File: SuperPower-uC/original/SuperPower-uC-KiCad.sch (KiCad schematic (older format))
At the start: 0 parts

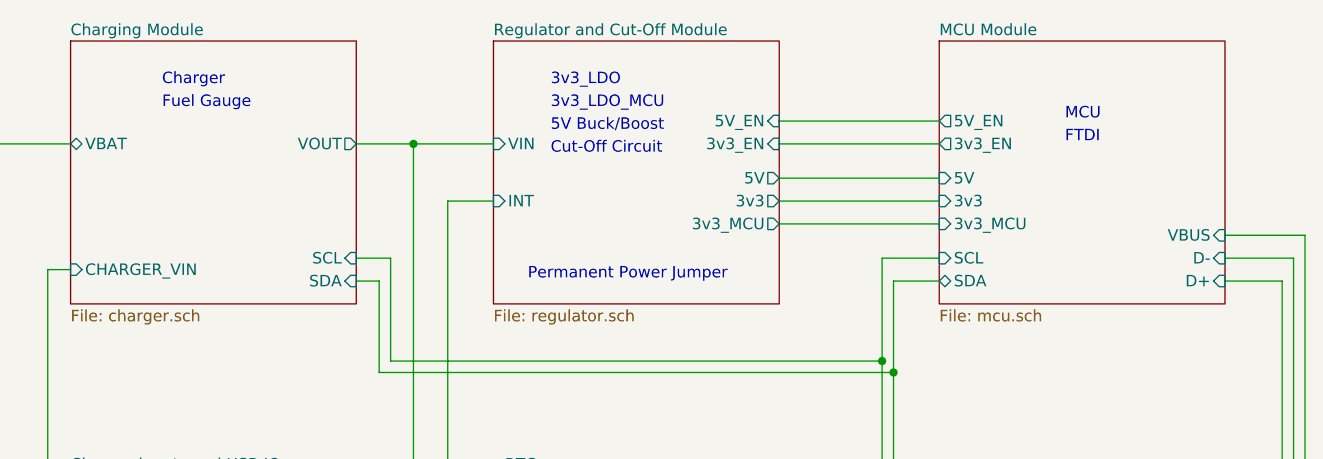
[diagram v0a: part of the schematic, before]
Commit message: Change some labels name and remove the hearders from the regulator sheet
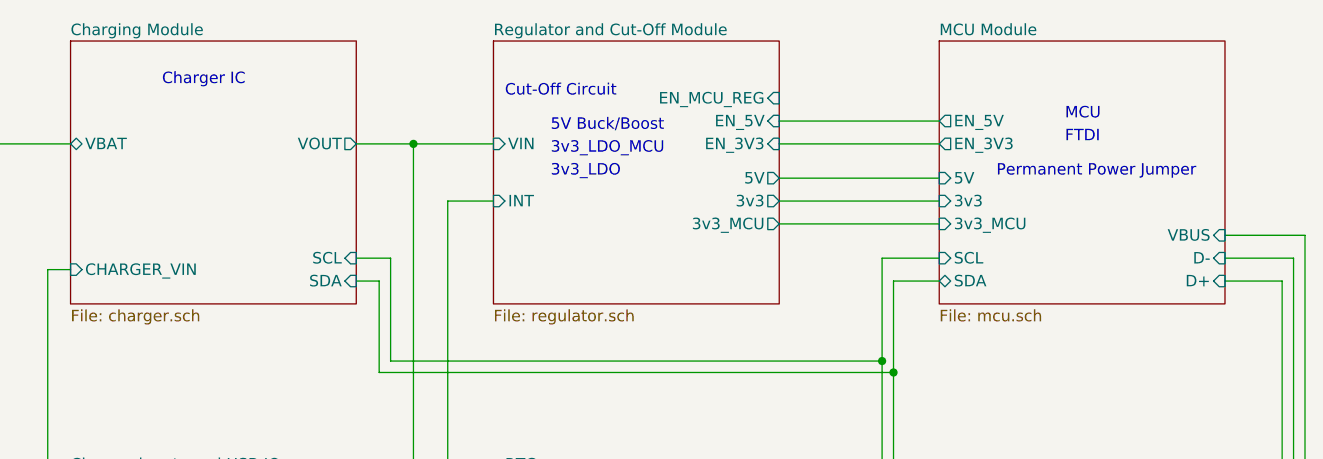
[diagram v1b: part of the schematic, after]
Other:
- note added: "Charger IC"
- note removed: "Charger"
- note removed: "Fuel Gauge"
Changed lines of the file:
@@
 F8 "5V" I L 6850 2700 50
 F9 "3v3" I L 6850 2800 50
-F10 "3v3_EN" O L 6850 2550 50
-F11 "5V_EN" O L 6850 2450 50
+F10 "EN_3V3" O L 6850 2550 50
+F11 "EN_5V" O L 6850 2450 50
 $EndSheet
 Wire Wire Line
@@
 Battery Protection
 Text Notes 3450 2300 0    50   ~ 0
-Charger
-Text Notes 3450 2400 0    50   ~ 0
-Fuel Gauge
-Text Notes 5150 2300 0    50   ~ 0
+Charger IC
+Text Notes 5150 2700 0    50   ~ 0
 3v3_LDO
-Text Notes 5150 2400 0    50   ~ 0
+Text Notes 5150 2600 0    50   ~ 0
 3v3_LDO_MCU
 Text Notes 5150 2500 0    50   ~ 0
@@
 Text Notes 5350 4450 0    50   ~ 0
 RTC
-Text Notes 5150 2600 0    50   ~ 0
+Text Notes 4950 2350 0    50   ~ 0
 Cut-Off Circuit
 Text Notes 3600 4350 0    50   ~ 0
@@
 Wire Wire Line
 	4700 5450 4700 4900
-Text Notes 5050 3150 0    50   ~ 0
+Text Notes 7100 2700 0    50   ~ 0
 Permanent Power Jumper
 Text Notes 7400 2550 0    50   ~ 0
@@
 F3 "3v3" O R 6150 2800 50
 F4 "5V" O R 6150 2700 50
-F5 "3v3_EN" I R 6150 2550 50
-F6 "5V_EN" I R 6150 2450 50
-F7 "3v3_MCU" O R 6150 2900 50
-F8 "VIN" I L 4900 2550 50
+F5 "3v3_MCU" O R 6150 2900 50
+F6 "VIN" I L 4900 2550 50
+F7 "EN_3V3" I R 6150 2550 50
+F8 "EN_5V" I R 6150 2450 50
+F9 "EN_MCU_REG" I R 6150 2350 50
 $EndSheet
 Wire Wire Line

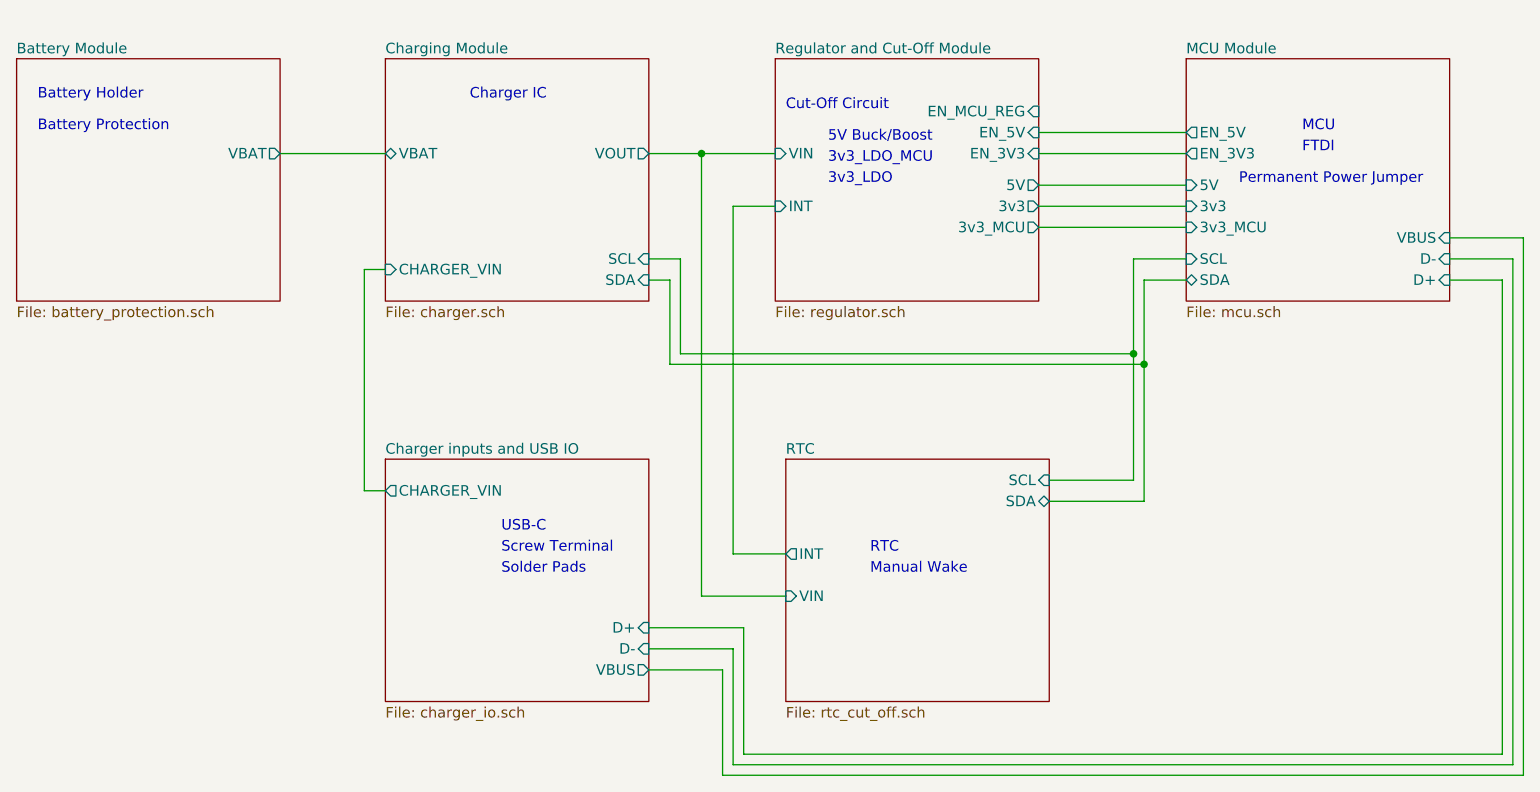
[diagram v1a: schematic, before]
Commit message: Rename labels
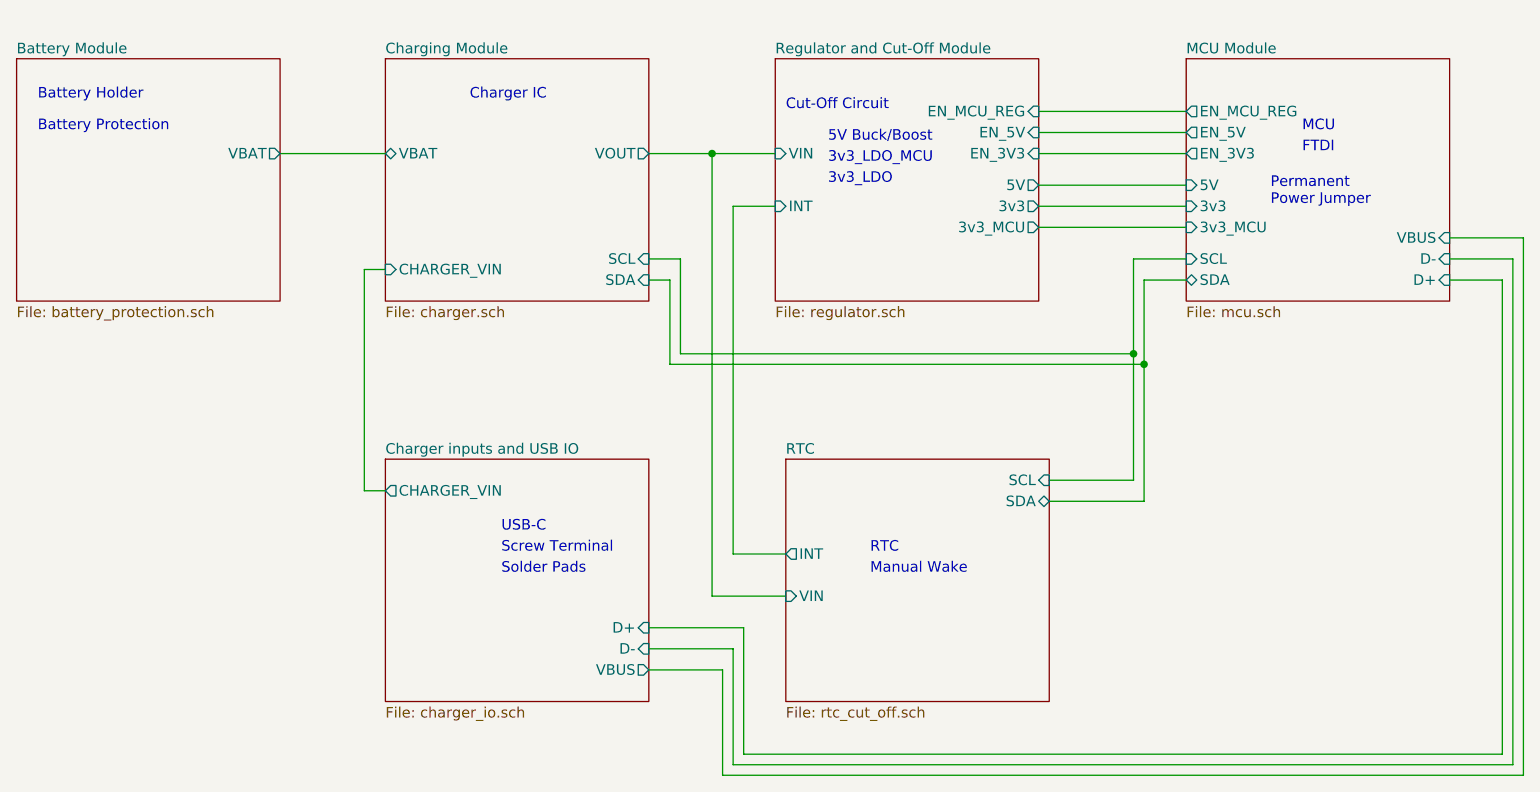
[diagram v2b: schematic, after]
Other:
- note added: "Permanent\nPower Jumper"
- note removed: "Permanent Power Jumper"
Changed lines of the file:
@@
 F10 "EN_3V3" O L 6850 2550 50
 F11 "EN_5V" O L 6850 2450 50
+F12 "EN_MCU_REG" O L 6850 2350 50
 $EndSheet
 Wire Wire Line
@@
 	6600 4100 6200 4100
 Wire Wire Line
-	4300 2550 4550 2550
+	4300 2550 4600 2550
 Wire Wire Line
-	4550 2550 4550 4650
+	4600 2550 4600 4650
 Wire Wire Line
-	4550 4650 4950 4650
+	4600 4650 4950 4650
 Wire Wire Line
 	4950 4450 4700 4450
@@
 Wire Wire Line
 	4700 5450 4700 4900
-Text Notes 7100 2700 0    50   ~ 0
-Permanent Power Jumper
+Text Notes 7250 2800 0    50   ~ 0
+Permanent\nPower Jumper
 Text Notes 7400 2550 0    50   ~ 0
 FTDI
 Wire Wire Line
-	4550 2550 4900 2550
-Connection ~ 4550 2550
+	4600 2550 4900 2550
+Connection ~ 4600 2550
 Wire Wire Line
 	6850 2550 6150 2550
@@
 Wire Wire Line
 	4650 5000 4300 5000
+Wire Wire Line
+	6150 2350 6850 2350
 $EndSCHEMATC

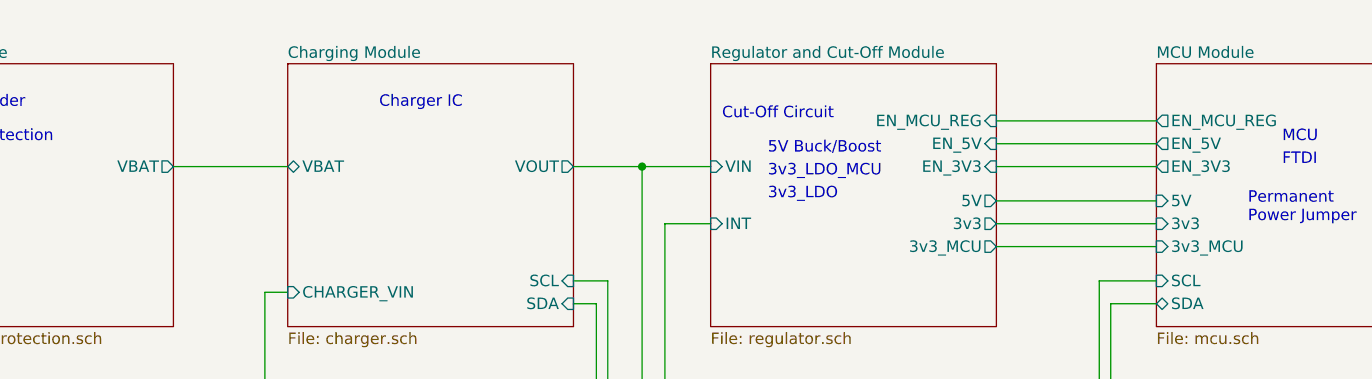
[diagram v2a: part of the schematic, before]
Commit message: Make VBAT bidirectionnal, add VIN to MCU sheet
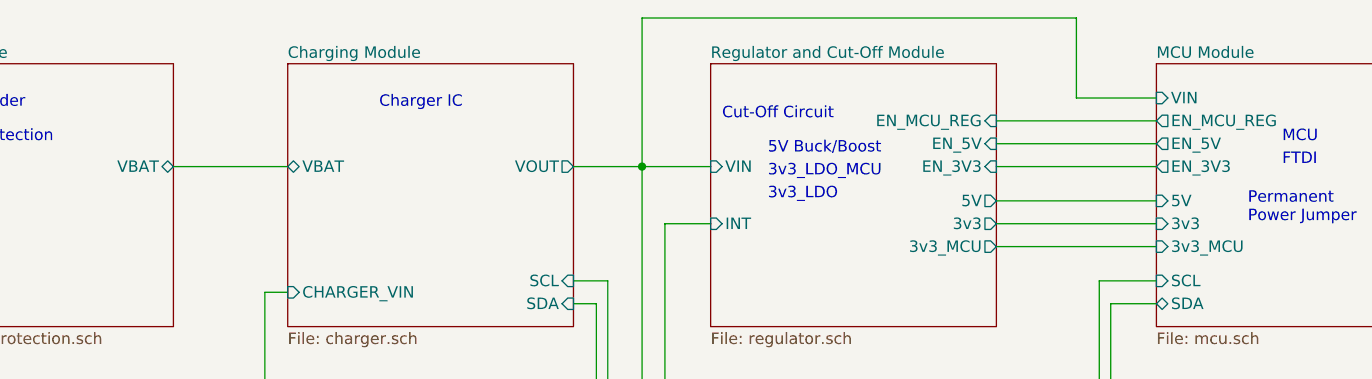
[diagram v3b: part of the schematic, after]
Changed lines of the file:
@@
 F0 "Battery Module" 50
 F1 "battery_protection.sch" 50
-F2 "VBAT" O R 2550 2550 50
+F2 "VBAT" B R 2550 2550 50
 $EndSheet
 $Sheet
@@
 F11 "EN_5V" O L 6850 2450 50
 F12 "EN_MCU_REG" O L 6850 2350 50
+F13 "VIN" I L 6850 2250 50
 $EndSheet
 Wire Wire Line
@@
 Wire Wire Line
 	6150 2350 6850 2350
+Wire Wire Line
+	4600 2550 4600 1900
+Wire Wire Line
+	4600 1900 6500 1900
+Wire Wire Line
+	6500 1900 6500 2250
+Wire Wire Line
+	6500 2250 6850 2250
 $EndSCHEMATC

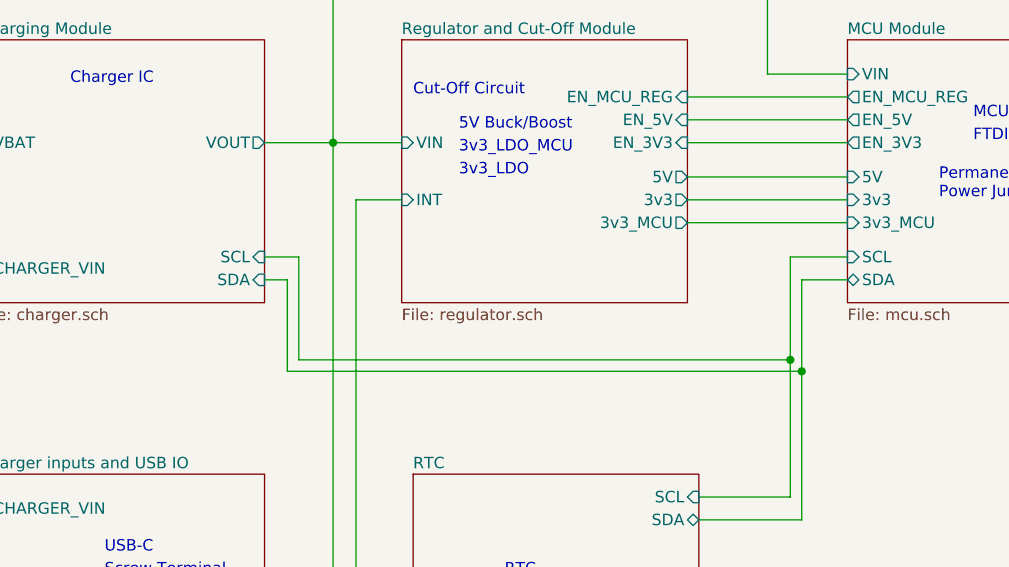
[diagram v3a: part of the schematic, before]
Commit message: Adds D_VCC to the charger IC
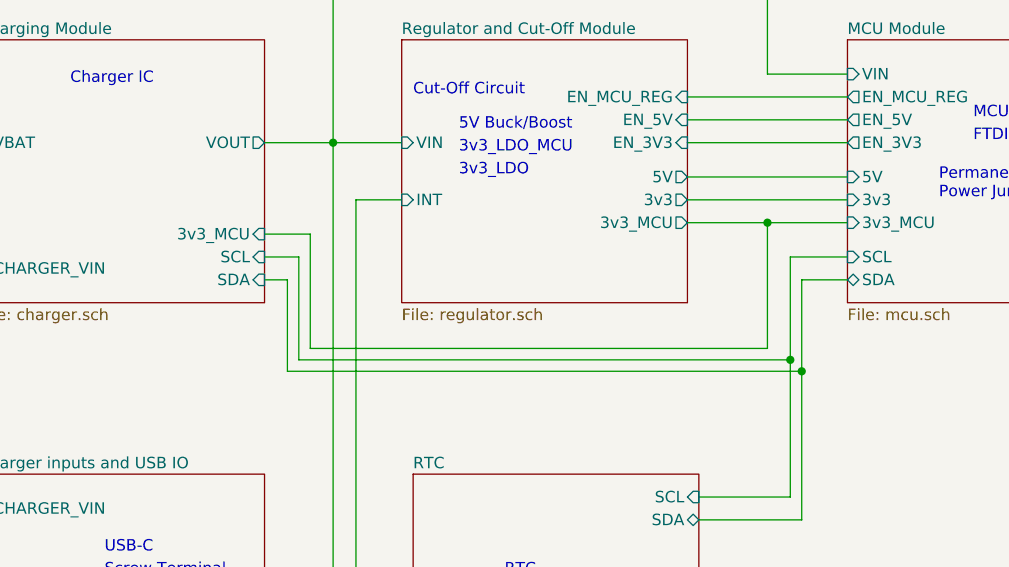
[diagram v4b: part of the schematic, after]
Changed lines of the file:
@@
 F5 "SCL" I R 4300 3050 50
 F6 "SDA" I R 4300 3150 50
+F7 "3v3_MCU" I R 4300 2950 50
 $EndSheet
 $Sheet
@@
 	2550 2550 3050 2550
 Wire Wire Line
-	6850 2900 6150 2900
+	6850 2900 6500 2900
 Wire Wire Line
 	6850 3150 6650 3150
@@
 Wire Wire Line
 	6500 2250 6850 2250
+Wire Wire Line
+	4300 2950 4500 2950
+Wire Wire Line
+	4500 2950 4500 3450
+Wire Wire Line
+	4500 3450 6500 3450
+Wire Wire Line
+	6500 3450 6500 2900
+Connection ~ 6500 2900
+Wire Wire Line
+	6500 2900 6150 2900
 $EndSCHEMATC
